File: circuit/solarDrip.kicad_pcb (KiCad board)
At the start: 2 copper layers, 57 x 50 mm, 24 parts, among them J1 solar_charger, J2 batt, J3 solar, J4 pump, J5 soil, J6 water, J7 USB_C_Receptacle_USB2.0_14P, Q1 2N7002K, Q2 2N7002K, Q3 FDN340P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

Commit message: run drc
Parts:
- moved J5 0.16 mm to (59.2, 81.7)
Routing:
- net vcc_usb: track 24.0 -> 30.4 mm
- net GND: track 0.00 -> 5.36 mm, vias 11 -> 12
- net vcc_pwr: track 31.0 -> 29.3 mm
- net bat_hi: track 37.2 -> 38.5 mm
- net solar_hi: track 42.0 -> 43.3 mm
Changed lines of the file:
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@@
 		(tags "SOT TO_SOT_SMD")
 		(property "Reference" "Q3"
-			(at 0 -2.4 90)
+			(at 0.24 -2.4 90)
 			(layer "F.SilkS")
 			(effects
@@
 		(tags "mounting hole 2.7mm no annular m2.5 din965")
 		(property "Reference" "H1"
-			(at 0 -3.35 0)
+			(at 3.8 0 0)
 			(layer "F.SilkS")
+			(hide yes)
 			(effects
 				(font
@@
 	(footprint "Connector_JST:JST_PH_S3B-PH-K_1x03_P2.00mm_Horizontal"
 		(layer "F.Cu")
-		(at 59.3594 81.562)
+		(at 59.25 81.685)
 		(descr "JST PH series connector, S3B-PH-K (http://www.jst-mfg.com/product/pdf/eng/ePH.pdf), generated with kicad-footprint-generator")
 		(tags "connector JST PH top entry")
@@
 		(tags "mounting hole 2.7mm no annular m2.5 din965")
 		(property "Reference" "H2"
-			(at 0 -3.35 0)
+			(at -3.8 0 0)
 			(layer "F.SilkS")
+			(hide yes)
 			(effects
 				(font
@@
 			(at 0 3.35 0)
 			(layer "F.Fab")
+			(hide yes)
 			(effects
 				(font
@@
 	)
 	(segment
-		(start 23.81 77.535)
-		(end 23.996 77.535)
-		(width 0.2)
-		(layer "B.Cu")
-		(net 0)
-	)
-	(segment
 		(start 45.205 76.4405)
 		(end 45.2027 76.4428)
@@
 	)
 	(via
+		(at 61.5 46.225)
+		(size 0.6)
+		(drill 0.3)
+		(layers "F.Cu" "B.Cu")
+		(free yes)
+		(net 3)
+	)
+	(via
 		(at 47.7196 56.9356)
 		(size 0.6)
@@
 	)
 	(segment
-		(start 61.3594 81.562)
-		(end 61.3594 79.0082)
+		(start 39.642 45.954)
+		(end 40.162 45.954)
+		(width 0.2)
+		(layer "B.Cu")
+		(net 3)
+	)
+	(segment
+		(start 33.242 45.954)
+		(end 33.242 46.783)
+		(width 0.2)
+		(layer "B.Cu")
+		(net 3)
+	)
+	(segment
+		(start 33.242 46.783)
+		(end 32.25 47.775)
+		(width 0.2)
+		(layer "B.Cu")
+		(net 3)
+	)
+	(segment
+		(start 39.642 45.954)
+		(end 39.642 46.567)
+		(width 0.2)
+		(layer "B.Cu")
+		(net 3)
+	)
+	(segment
+		(start 39.642 46.567)
+		(end 40.45 47.375)
+		(width 0.2)
+		(layer "B.Cu")
+		(net 3)
+	)
+	(segment
+		(start 40.162 45.954)
+		(end 40.762 45.354)
+		(width 0.2)
+		(layer "B.Cu")
+		(net 3)
+	)
+	(segment
+		(start 67.894785 56.807215)
+		(end 67.894785 48.848831)
 		(width 0.2)
 		(layer "F.Cu")
@@
 	)
 	(segment
-		(start 74.262285 66.105315)
-		(end 74.262285 63.174715)
+		(start 61.25 79.1176)
+		(end 74.262285 66.105315)
 		(width 0.2)
 		(layer "F.Cu")
@@
 	)
 	(segment
-		(start 74.262285 63.174715)
-		(end 67.894785 56.807215)
+		(start 74.262285 66.105315)
+		(end 74.262285 63.174715)
 		(width 0.2)
 		(layer "F.Cu")
@@
 	)
 	(segment
-		(start 61.3594 79.0082)
-		(end 74.262285 66.105315)
+		(start 61.25 81.685)
+		(end 61.25 79.1176)
 		(width 0.2)
 		(layer "F.Cu")
@@
 	)
 	(segment
-		(start 67.894785 56.807215)
-		(end 67.894785 48.848831)
+		(start 74.262285 63.174715)
+		(end 67.894785 56.807215)
 		(width 0.2)
 		(layer "F.Cu")
@@
 	)
 	(segment
-		(start 62.814785 48.848831)
-		(end 62.765969 48.848831)
+		(start 54.2408 59.2342)
+		(end 54.2408 81.689)
 		(width 0.4)
 		(layer "B.Cu")
@@
 	)
 	(segment
-		(start 56.6422 79.2876)
-		(end 54.2408 81.689)
+		(start 63.25 81.685)
+		(end 63.25 81.4526)
 		(width 0.4)
 		(layer "B.Cu")
@@
 	)
 	(segment
-		(start 61.085 79.2876)
-		(end 56.6422 79.2876)
+		(start 63.25 81.4526)
+		(end 61.085 79.2876)
 		(width 0.4)
 		(layer "B.Cu")
@@
 	)
 	(segment
-		(start 62.765969 48.848831)
-		(end 54.2408 57.374)
+		(start 56.6422 79.2876)
+		(end 54.2408 81.689)
 		(width 0.4)
 		(layer "B.Cu")
@@
 	)
 	(segment
-		(start 63.3594 81.562)
-		(end 61.085 79.2876)
+		(start 61.085 79.2876)
+		(end 56.6422 79.2876)
 		(width 0.4)
 		(layer "B.Cu")
@@
 	)
 	(segment
-		(start 54.2408 57.374)
-		(end 54.2408 81.689)
+		(start 62.814785 50.660215)
+		(end 54.2408 59.2342)
+		(width 0.4)
+		(layer "B.Cu")
+		(net 6)
+	)
+	(segment
+		(start 62.814785 48.848831)
+		(end 62.814785 50.660215)
 		(width 0.4)
 		(layer "B.Cu")
@@
 	(segment
 		(start 45.0272 57.958486)
-		(end 56.286855 46.698831)
+		(end 57.860686 45.125)
 		(width 0.2)
 		(layer "F.Cu")
@@
 	)
 	(segment
-		(start 69.309031 46.698831)
-		(end 70.434785 47.824585)
+		(start 45.0272 61.758501)
+		(end 45.0272 57.958486)
 		(width 0.2)
 		(layer "F.Cu")
@@
 	)
 	(segment
-		(start 43.2072 61.758501)
-		(end 45.0272 61.758501)
+		(start 70.434785 47.824585)
+		(end 70.434785 48.848831)
 		(width 0.2)
 		(layer "F.Cu")
@@
 	)
 	(segment
-		(start 45.0272 61.758501)
-		(end 45.0272 57.958486)
+		(start 43.2072 61.758501)
+		(end 45.0272 61.758501)
 		(width 0.2)
 		(layer "F.Cu")
@@
 	)
 	(segment
-		(start 70.434785 47.824585)
-		(end 70.434785 48.848831)
+		(start 67.7352 45.125)
+		(end 70.434785 47.824585)
 		(width 0.2)
 		(layer "F.Cu")
@@
 	)
 	(segment
-		(start 56.286855 46.698831)
-		(end 69.309031 46.698831)
+		(start 57.860686 45.125)
+		(end 67.7352 45.125)
 		(width 0.2)
 		(layer "F.Cu")
@@
 	(segment
 		(start 41.0394 61.3806)
-		(end 56.121169 46.298831)
+		(end 57.695 44.725)
 		(width 0.2)
 		(layer "F.Cu")
@@
 	)
 	(segment
-		(start 56.121169 46.298831)
-		(end 71.220431 46.298831)
+		(start 41.0394 61.758501)
+		(end 41.0394 61.3806)
 		(width 0.2)
 		(layer "F.Cu")
@@
 	)
 	(segment
-		(start 72.974785 48.053185)
-		(end 72.974785 48.848831)
+		(start 69.6466 44.725)
+		(end 72.974785 48.053185)
 		(width 0.2)
 		(layer "F.Cu")
@@
 	)
 	(segment
-		(start 39.0844 61.758501)
-		(end 41.0394 61.758501)
+		(start 72.974785 48.053185)
+		(end 72.974785 48.848831)
 		(width 0.2)
 		(layer "F.Cu")
@@
 	)
 	(segment
-		(start 71.220431 46.298831)
-		(end 72.974785 48.053185)
+		(start 39.0844 61.758501)
+		(end 41.0394 61.758501)
 		(width 0.2)
 		(layer "F.Cu")
@@
 	)
 	(segment
-		(start 41.0394 61.758501)
-		(end 41.0394 61.3806)
+		(start 57.695 44.725)
+		(end 69.6466 44.725)
 		(width 0.2)
 		(layer "F.Cu")
@@
 	)
 	(segment
-		(start 23.849696 72.047126)
-		(end 23.9198 72.11723)
-		(width 0.6)
-		(layer "F.Cu")
-		(net 21)
-	)
-	(segment
 		(start 28.6696 54.6671)
 		(end 32.1392 51.1975)
@@
 	)
 	(segment
-		(start 23.9198 72.11723)
-		(end 23.9198 73.6488)
-		(width 0.6)
-		(layer "F.Cu")
-		(net 21)
-	)
-	(segment
-		(start 23.9198 73.6488)
-		(end 23.996 73.725)
-		(width 0.6)
-		(layer "F.Cu")
-		(net 21)
-	)
-	(segment
 		(start 27.8875 55.4492)
 		(end 23.996 55.4492)
@@
 	)
 	(segment
-		(start 28.6696 65.2922)
-		(end 23.849696 70.112104)
+		(start 28.6696 65.2414)
+		(end 28.6696 67.227222)
 		(width 0.6)
 		(layer "B.Cu")
@@
 	)
 	(segment
-		(start 23.849696 70.112104)
+		(start 28.6696 67.227222)
 		(end 23.849696 72.047126)
 		(width 0.6)
@@
 	)
 	(segment
-		(start 28.6696 65.2414)
-		(end 28.6696 65.2922)
-		(width 0.6)
-		(layer "B.Cu")
-		(net 21)
-	)
-	(segment
 		(start 34.0392 49.4172)
 		(end 34.0392 51.1975)
@@
 	)
 	(segment
-		(start 41.395 48.2234)
-		(end 40.3914 48.2234)
+		(start 38.842 45.954)
+		(end 38.842 46.774)
 		(width 0.2)
 		(layer "B.Cu")
@@
 	)
 	(segment
-		(start 42.9444 49.7728)
-		(end 41.395 48.2234)
+		(start 38.642 45.034)
+		(end 34.242 45.034)
 		(width 0.2)
 		(layer "B.Cu")
@@
 	)
 	(segment
-		(start 40.3914 48.2234)
-		(end 38.842 46.674)
+		(start 34.242 45.754)
+		(end 34.042 45.954)
+		(width 0.2)
+		(layer "B.Cu")
+		(net 22)
+	)
+	(segment
+		(start 38.842 45.954)
+		(end 38.642 45.754)
+		(width 0.2)
+		(layer "B.Cu")
+		(net 22)
+	)
+	(segment
+		(start 38.842 46.774)
+		(end 40.443 48.375)
 		(width 0.2)
 		(layer "B.Cu")
@@
 	)
 	(segment
-		(start 38.842 46.674)
-		(end 38.842 45.954)
+		(start 40.443 48.375)
+		(end 41.3434 48.375)
 		(width 0.2)
 		(layer "B.Cu")
@@
 	)
 	(segment
-		(start 42.9444 49.976)
-		(end 42.9444 49.7728)
+		(start 38.642 45.754)
+		(end 38.642 45.034)
+		(width 0.2)
+		(layer "B.Cu")
+		(net 22)
+	)
+	(segment
+		(start 41.3434 48.375)
+		(end 42.9444 49.976)
 		(width 0.2)
 		(layer "B.Cu")
@@
 	)
 	(segment
+		(start 34.242 45.034)
+		(end 34.242 45.754)
+		(width 0.2)
+		(layer "B.Cu")
+		(net 22)
+	)
+	(segment
 		(start 37.8771 50.2427)
 		(end 37.8771 51.4861)
@@
 		(polygon
 			(pts
-				(xy 82.67 43.2196) (xy 83.0764 42.9656) (xy 83.2796 70.9818) (xy 73.0434 61.152) (xy 73.0688 51.6016)
+				(xy 74.25 50.225) (xy 76.75 50.225) (xy 76.75 46.975) (xy 82.75 46.975) (xy 82.75 67.225) (xy 76.75 67.225)
+				(xy 76.75 62.725) (xy 74.25 62.725)
 			)
 		)

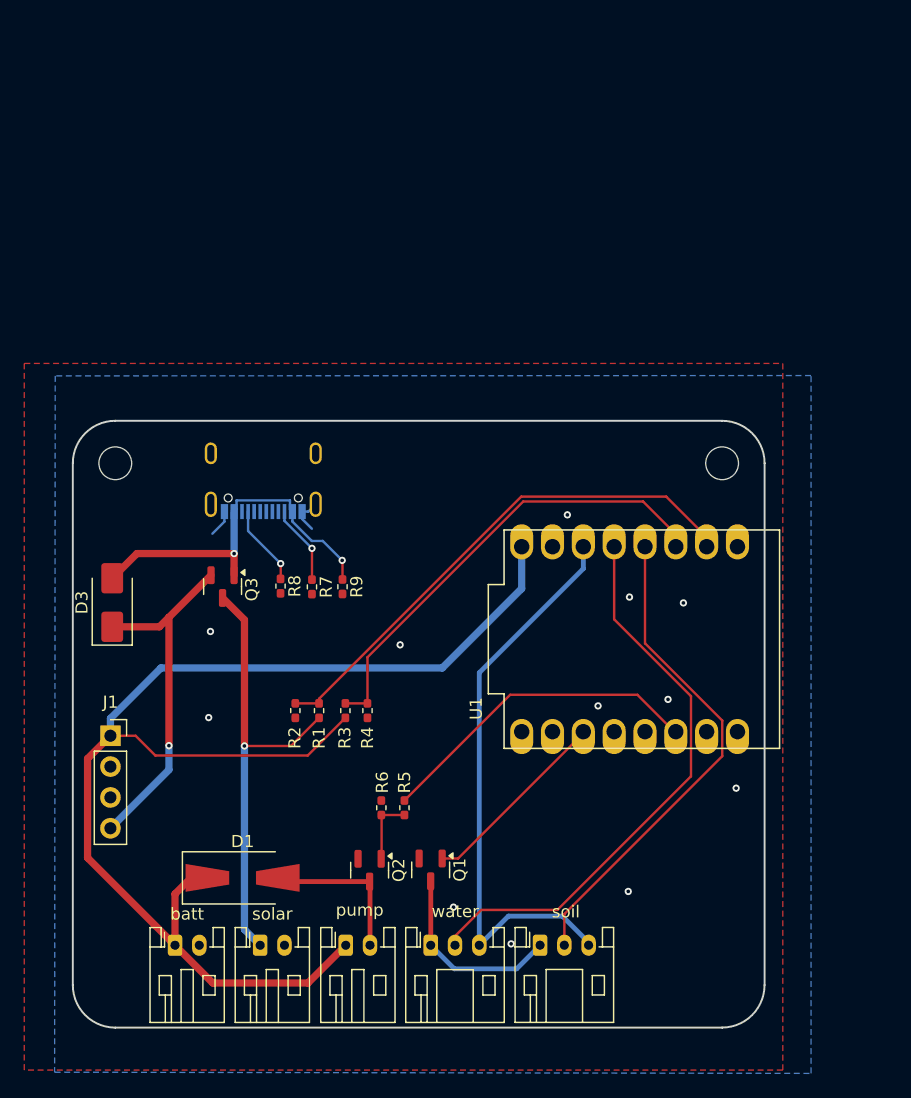
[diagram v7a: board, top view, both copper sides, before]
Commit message: vias, silkscreen, add usb_prw, logos and serials
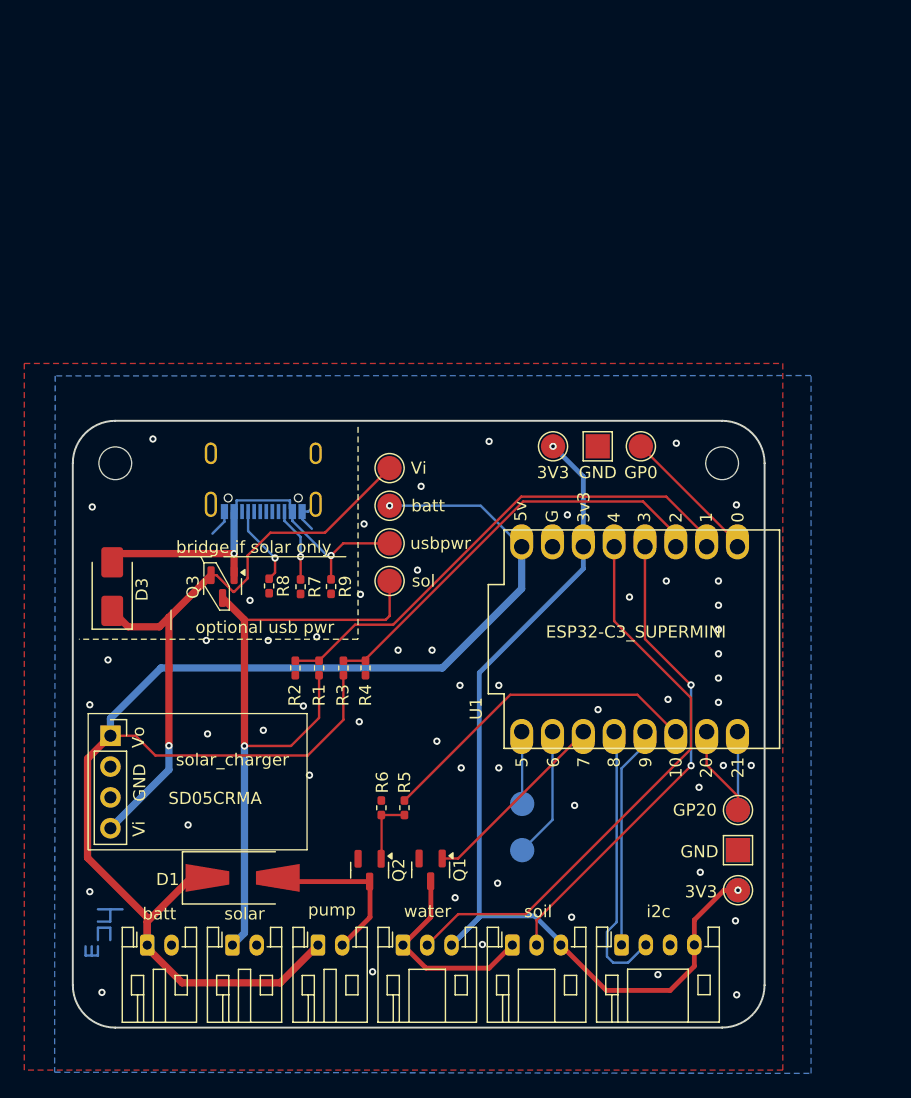
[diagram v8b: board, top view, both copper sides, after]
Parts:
- added J8: i2c, Connector_JST:JST_PH_S4B-PH-K_1x04_P2.00mm_Horizontal, F.Cu at (66.0, 81.7)
- added REF**: muccc_logo, my_footprints:muccc_logo, B.Cu at (24.9, 78.7)
- added TP1: batt, TestPoint:TestPoint_Pad_D2.0mm, F.Cu at (46.9, 45.5)
- added TP10: GP0, TestPoint:TestPoint_Pad_D2.0mm, F.Cu at (67.6, 40.6)
- added TP11: GP5, TestPoint:TestPoint_Pad_D2.0mm, B.Cu at (57.8, 70.0)
- added TP12: GP6, TestPoint:TestPoint_Pad_D2.0mm, B.Cu at (57.8, 73.9)
- added TP13: GP21, TestPoint:TestPoint_Pad_D2.0mm, B.Cu at (75.6, 70.5)
- added TP14: GP20, TestPoint:TestPoint_Pad_D2.0mm, F.Cu at (75.6, 70.5)
- added TP15: usbpwr, TestPoint:TestPoint_Pad_D2.0mm, F.Cu at (46.9, 48.6)
- added TP2: sol, TestPoint:TestPoint_Pad_D2.0mm, F.Cu at (46.9, 51.7)
- added TP3: Vi, TestPoint:TestPoint_Pad_D2.0mm, F.Cu at (46.9, 42.4)
- added TP4: 3V3, TestPoint:TestPoint_Pad_D2.0mm, B.Cu at (75.6, 77.2)
- added TP5: 3V3, TestPoint:TestPoint_Pad_D2.0mm, F.Cu at (75.6, 77.2)
- added TP6: 3V3, TestPoint:TestPoint_Pad_D2.0mm, F.Cu at (60.3, 40.6)
- added TP7: GND, TestPoint:TestPoint_Pad_2.0x2.0mm, F.Cu at (64.0, 40.6)
- added TP8: GND, TestPoint:TestPoint_Pad_2.0x2.0mm, B.Cu at (75.6, 73.9)
- added TP9: GND, TestPoint:TestPoint_Pad_2.0x2.0mm, F.Cu at (75.6, 73.9)
- moved R3 3.52 mm to (43.0, 58.8)
- moved R4 3.52 mm to (44.9, 58.8)
- moved R1 3.52 mm to (41.0, 58.8)
- moved R2 3.52 mm to (39.1, 58.8)
- moved J3 2.29 mm to (33.9, 81.7)
- moved J4 2.29 mm to (40.9, 81.7)
- moved J2 2.29 mm to (26.9, 81.7)
- moved J5 2.29 mm to (57.0, 81.7)
- moved J6 2.29 mm to (48.0, 81.7)
- moved D3 1.31 mm to (24.0, 52.1)
- moved R8 0.94 mm to (36.9, 52.1)
- moved R7 0.94 mm to (39.5, 52.1)
- moved R9 0.94 mm to (42.0, 52.1)
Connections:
- U1 pad 0: unconnected-(U1-GPIO0-Pad0) -> gpio0
- U1 pad 20: unconnected-(U1-GPIO20-Pad20) -> gpio20
- U1 pad 21: unconnected-(U1-GPIO21-Pad21) -> gpio21
- U1 pad 5: unconnected-(U1-GPIO5-Pad5) -> gpio5
- U1 pad 6: unconnected-(U1-GPIO6-Pad6) -> gpio6
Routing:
- net vcc_logic: track 47.5 -> 79.6 mm, vias 0 -> 2
- net scl: track 0.00 -> 23.0 mm
- net vcc_pwr: track 29.3 -> 51.0 mm
- net sda: track 0.00 -> 18.4 mm
- net vcc_solar: track 37.0 -> 55.4 mm
- net vcc_battery: track 109.6 -> 125.6 mm, vias 0 -> 1
- net gpio0: track 0.00 -> 11.6 mm
- net gpio6: track 0.00 -> 10.8 mm
- net gpio20: track 0.00 -> 7.53 mm
- net gpio21: track 0.00 -> 6.48 mm
- net gpio5: track 0.00 -> 5.97 mm
- net vcc_usb: track 30.4 -> 34.3 mm
- net bat_hi: track 38.5 -> 35.0 mm
- net solar_hi: track 43.3 -> 41.7 mm
- net in-a_moisture: track 40.9 -> 39.7 mm, vias 0 -> 2
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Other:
- board text added: "0"
- board text added: "1"
- board text added: "10"
- board text added: "2"
- board text added: "20"
- board text added: "21"
- board text added: "3"
- board text added: "3v3"
- board text added: "4"
- board text added: "5"
- board text added: "5v"
- board text added: "6"
- board text added: "7"
- board text added: "8"
- board text added: "9"
- board text added: "G"
- board text added: "GND"
- board text added: "JLCJLCJLCJLCJLC"
- board text added: "SD05CRMA"
- board text added: "SolarDripIrigation v0.1 9R 05/2024"
- board text added: "Vi"
- board text added: "Vo"
- board text added: "bridge if solar only"
- board text added: "optional usb pwr"
